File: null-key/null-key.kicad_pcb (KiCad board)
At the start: 2 copper layers, 115.5 x 29.5 mm, 10 parts, among them J1 Conn_01x03, J2 Conn_02x03, U1 ProMicroC

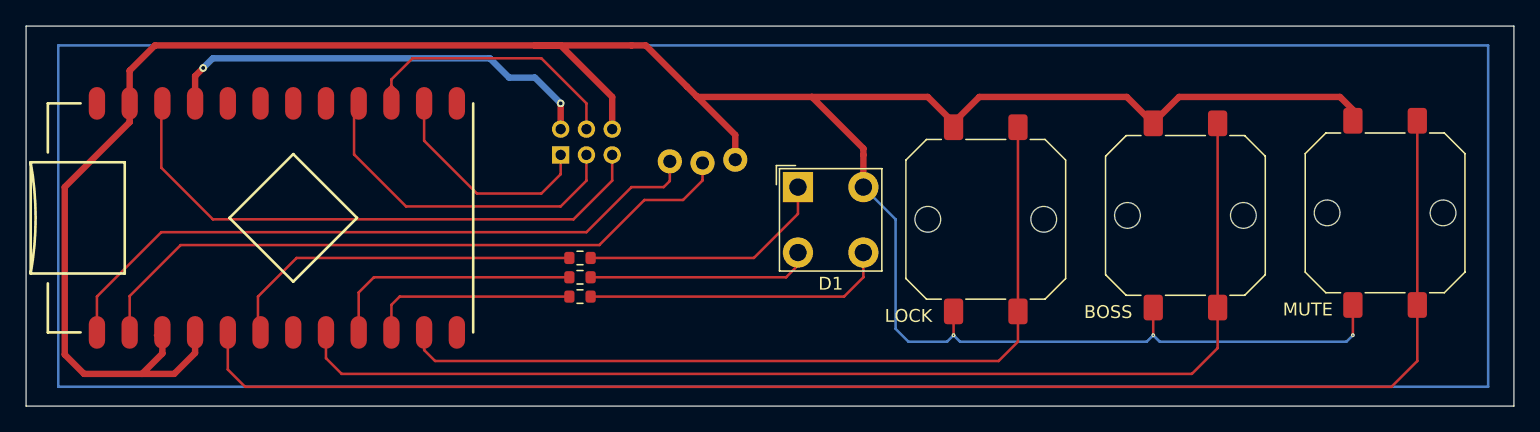
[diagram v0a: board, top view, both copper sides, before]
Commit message: fixed cross pins from schematic
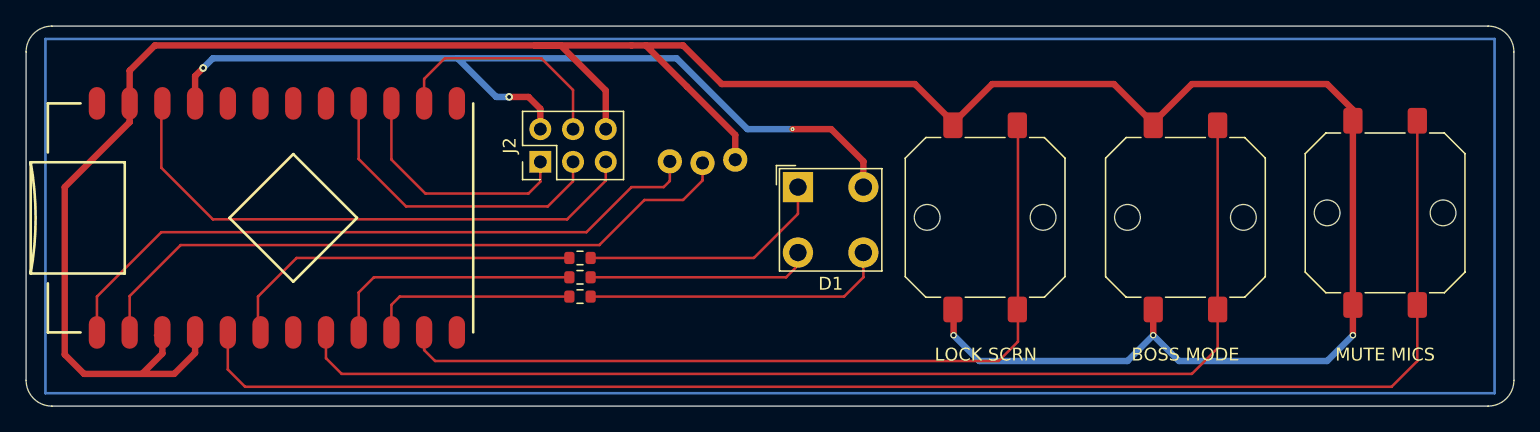
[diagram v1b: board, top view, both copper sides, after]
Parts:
- removed BOSS: SW2, Button_Switch_SMD:SW_Push_1P1T_NO_CK_PTS125Sx73PSMTR
- removed LOCK: SW3, Button_Switch_SMD:SW_Push_1P1T_NO_CK_PTS125Sx73PSMTR
- removed MUTE: SW1, Button_Switch_SMD:SW_Push_1P1T_NO_CK_PTS125Sx73PSMTR
- added BOSS MODE: SW_Push, Button_Switch_SMD:SW_Push_1P1T_NO_CK_PTS125Sx73PSMTR, F.Cu at (117.0, 68.8)
- added LOCK SCRN: SW_Push, Button_Switch_SMD:SW_Push_1P1T_NO_CK_PTS125Sx73PSMTR, F.Cu at (101.5, 68.8)
- added MUTE MICS: SW_Push, Button_Switch_SMD:SW_Push_1P1T_NO_CK_PTS125Sx73PSMTR, F.Cu at (132.5, 68.5)
- J2: value Conn_02x03 -> Conn_02x03_Odd_Even; footprint PCM_SparkFun-Connector:2x03_P2.00mm_NoSilk -> Connector_PinHeader_2.54mm:PinHeader_2x03_P2.54mm_Vertical
- moved J2 3.90 mm to (66.9, 64.5)
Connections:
- net Net-(U1-RST) renamed /TC3 RESET
- D1 pad 4: GND -> +5V
- J2 pad 1: /D16 MOSI -> /D14 MISO
- J2 pad 4: /D14 MISO -> /D16 MOSI
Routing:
- net +5V: track 34.7 -> 69.7 mm, vias 2 -> 3
- net /D14 MISO: track 23.3 -> 19.9 mm
- net GND: track 224.2 -> 222.2 mm
- net /D15 SCK/CLOCK: track 26.6 -> 25.2 mm
- net /TC3 RESET: track 44.9 -> 43.9 mm
- net /D16 MOSI: track 17.5 -> 18.2 mm
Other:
- outline, holes or cut-outs redrawn
